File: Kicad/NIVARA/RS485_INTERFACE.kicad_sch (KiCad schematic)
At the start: 0 parts

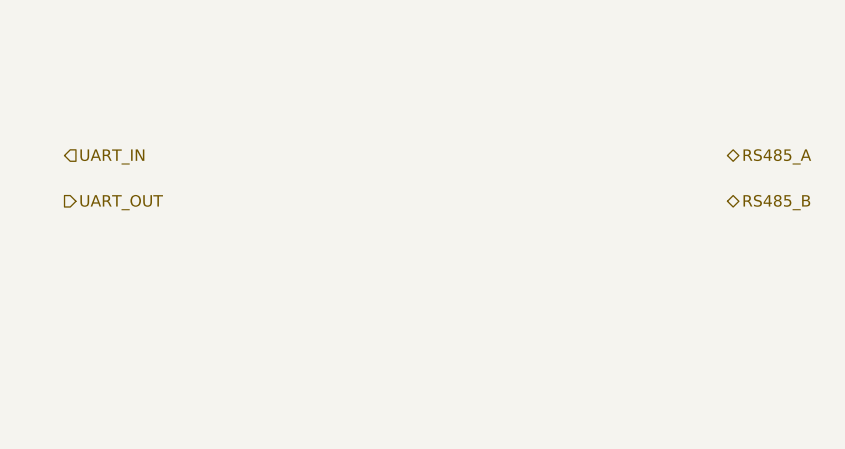
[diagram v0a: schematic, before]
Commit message: RS-485 Update
RS-485 Isolated circuit updated. Created new symbol and footprint for the YLPTEC RSM3485ECHT IC.
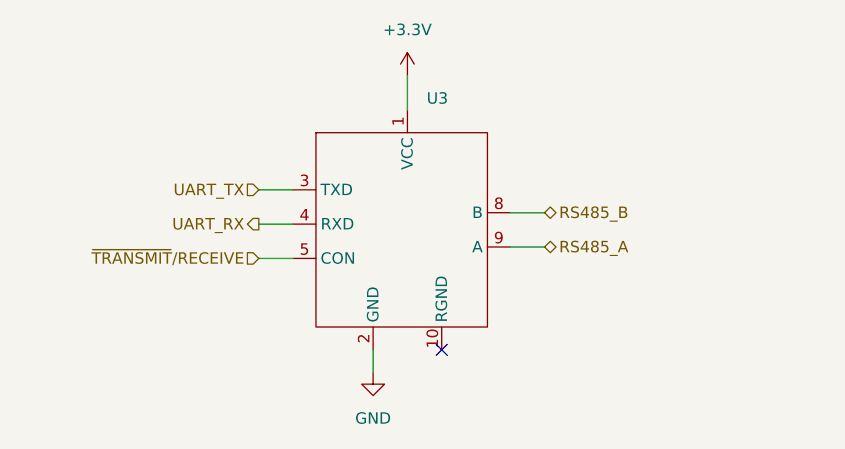
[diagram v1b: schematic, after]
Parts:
- added U3: ~, Riqi_Parts:YLPTEC RSM3485ECHT, symbol Riqi_Parts:YLPTEC_RSM3485ECHT
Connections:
- net RS485_A: now also U3.9 (A)
- net RS485_B: now also U3.8 (B)
- new net +3.3V: U3.1 (VCC)
- new net GND: U3.2 (GND)
- new net UART_RX: U3.4 (RXD)
- new net UART_TX: U3.3 (TXD)
- new net ~{TRANSMIT}/RECEIVE: U3.5 (CON)
- no-connect marks 0 -> 1

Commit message: Silly little things
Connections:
- net ~{TRANSMIT}/RECEIVE renamed ~{TX}/RX
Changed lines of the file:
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@@
 		)
 	)
-	(hierarchical_label "~{TRANSMIT}{slash}RECEIVE"
+	(hierarchical_label "~{TX}{slash}RX"
 		(shape input)
 		(at 104.14 76.2 180)
